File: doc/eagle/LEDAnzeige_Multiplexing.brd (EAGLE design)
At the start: 85.1 x 117.1 mm, 20 parts, among them P1-O8RIGHT TD620831A, P1-P8LEFT TD620831A, U1 SN74HC595N, U2 SN74HC595N, U3 SN74HC595N

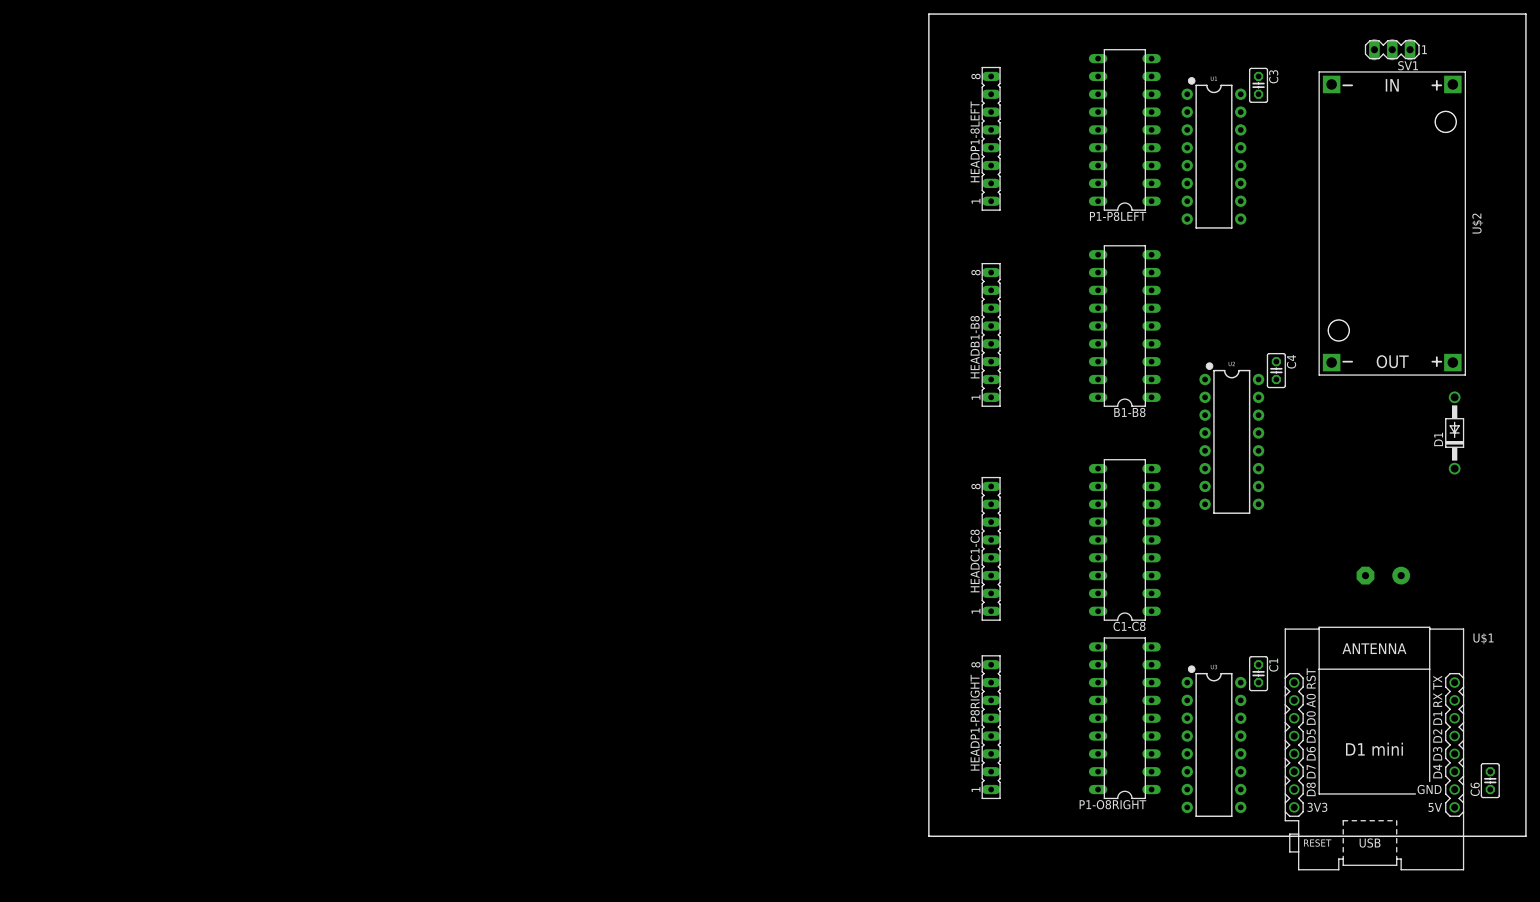
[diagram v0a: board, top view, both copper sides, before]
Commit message: Schematic updated + Refactoring
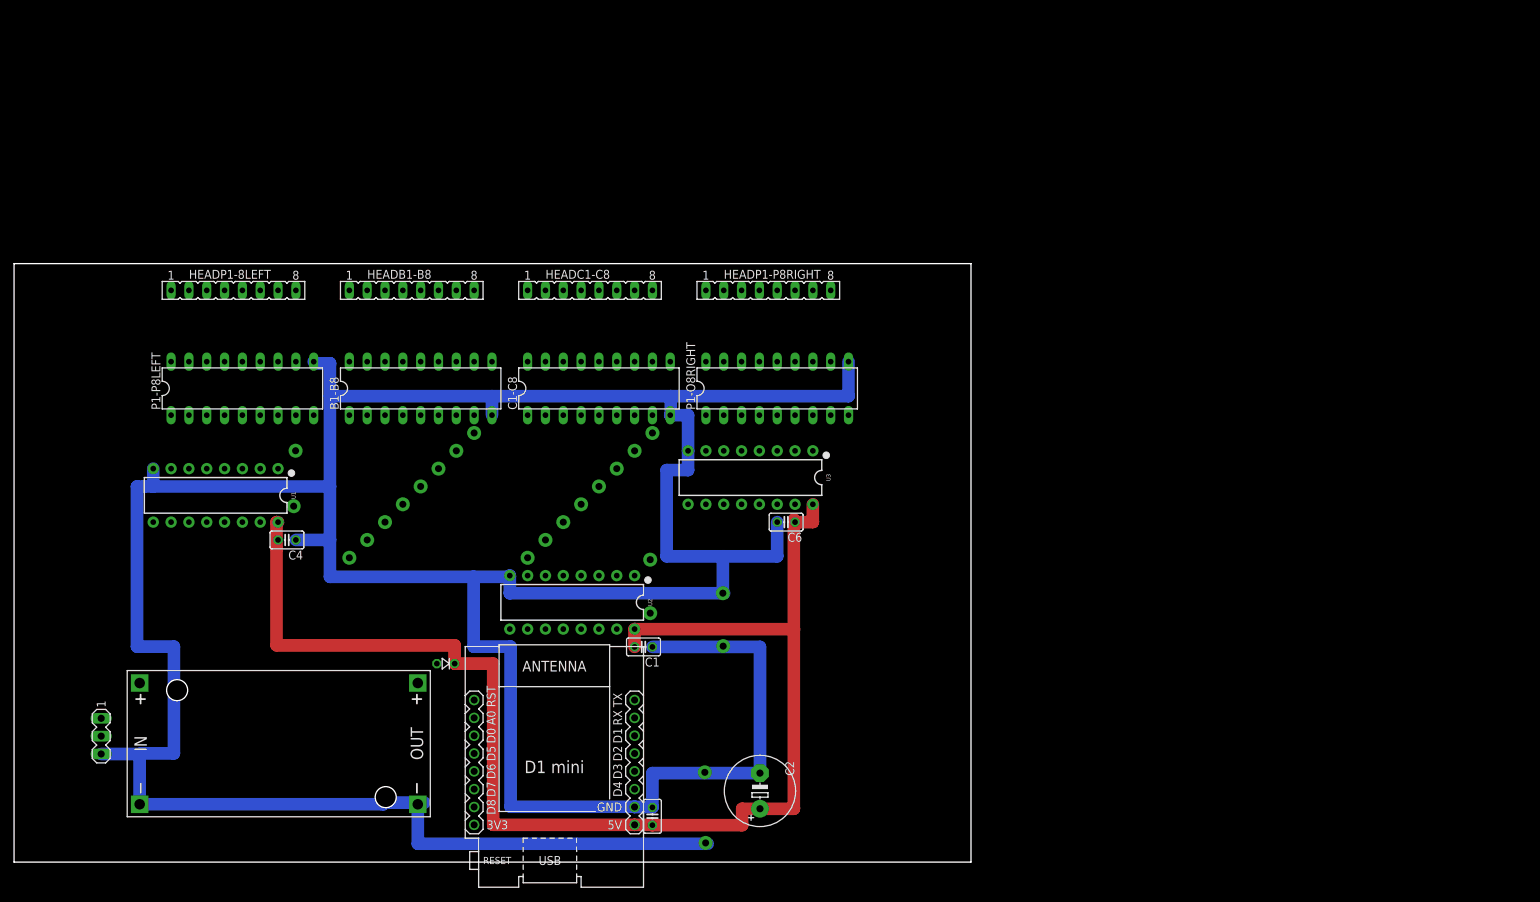
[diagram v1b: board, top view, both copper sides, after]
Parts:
- removed D1: 1N4004, diode:DO41-10
- added 1N4007: (no value), diode:D-2.5
- P1-O8RIGHT, P1-P8LEFT: value TD620831A -> TD627832A
- moved SV1 208.3 mm to (-67.1, 16.5), turned to 270 degrees
- moved U$2 175.1 mm to (-41.8, 15.4), turned to 0 degrees
- moved U1 150.2 mm to (-50.8, 50.8), turned to 180 degrees
- moved C4 143.0 mm to (-40.6, 44.5), turned to 180 degrees
- moved C3 135.3 mm to (11.4, 5.08)
- moved P1-P8LEFT 131.0 mm to (-47.0, 66.0), turned to 0 degrees
- moved U$1 116.9 mm to (-2.54, 12.1)
- moved HEADP1-8LEFT 110.1 mm to (-48.3, 80.0), turned to 0 degrees
- moved C6 106.9 mm to (30.5, 47.0), turned to 180 degrees
- moved B1-B8 100.7 mm to (-21.6, 66.0), turned to 0 degrees
- moved U2 96.7 mm to (0.00, 35.6), turned to 180 degrees
- moved C2 94.0 mm to (26.8, 8.69), flipped to the top, turned to 90 degrees
- moved C1 87.7 mm to (10.2, 29.2), turned to 180 degrees
- moved HEADB1-B8 82.8 mm to (-22.9, 80.0), turned to 0 degrees
- moved C1-C8 78.0 mm to (3.81, 66.0), turned to 0 degrees
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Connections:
- removed net N$38: U$1.JP2.3, U2.12
- removed net N$79: U$1.JP1.3, U1.11, U3.11
- new net N$60: U$1.JP2.4, U2.12
- new net N$76: U$1.JP1.5, U1.11, U3.11
- net 24V: now also P1-O8RIGHT.9, P1-P8LEFT.9; no longer P1-O8RIGHT.10, P1-P8LEFT.10
- net GND: now also P1-O8RIGHT.10, P1-P8LEFT.10; no longer P1-O8RIGHT.9, P1-P8LEFT.9
- net N$34: now also U$1.JP1.3; no longer U$1.JP1.5
- net N$37: now also U$1.JP2.3; no longer U$1.JP2.5
- net N$69: now also 1N4007.A; no longer D1.A
- net N$80: now also U$1.JP2.5; no longer U$1.JP2.4
- net VCC: now also 1N4007.C; no longer D1.C
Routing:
- net GND: track 0.00 -> 463.9 mm
- net VCC: track 0.00 -> 191.0 mm
- net N$63: track 0.00 -> 122.6 mm, vias 0 -> 6
- net 24V: track 0.00 -> 85.1 mm
- net N$76: track 0.00 -> 76.2 mm
- net N$74: track 0.00 -> 71.1 mm
- net N$34: track 0.00 -> 63.5 mm
- net N$61: track 0.00 -> 53.3 mm
- net N$64: track 0.00 -> 50.8 mm, vias 0 -> 3
- net N$3: track 0.00 -> 38.1 mm
- net N$4: track 0.00 -> 35.6 mm
- net N$6: track 20.3 -> 55.9 mm, vias 0 -> 1
- net N$1: track 20.3 -> 53.3 mm, vias 0 -> 1
- net N$80: track 0.00 -> 33.0 mm
- net N$60: track 0.00 -> 27.9 mm
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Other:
- board size 85.1 x 117.1 mm -> 136.3 x 85.3 mm

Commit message: Board updated
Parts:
- moved SV1 61.2 mm to (-69.8, 77.7), turned to 0 degrees
- moved C6 5.08 mm to (30.5, 41.9)
- moved C1 2.54 mm to (10.2, 26.7)
- moved U2 2.54 mm to (0.00, 33.0)
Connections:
- net GND: now also U1.13, U2.13, U3.13
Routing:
- net N$61: track 53.3 -> 91.1 mm
- net N$5: track 10.2 -> 35.6 mm
- net GND: track 463.9 -> 479.1 mm
- net 24V: track 85.1 -> 94.8 mm
- net N$63: track 122.6 -> 127.7 mm
- net N$80: track 33.0 -> 30.4 mm
- net N$7: track 43.2 -> 45.7 mm
- net N$60: track 27.9 -> 25.4 mm
- net N$6: track 55.9 -> 58.4 mm
- net N$4: track 35.6 -> 38.1 mm
- net N$37: track 20.3 -> 17.7 mm
- net N$36: track 13.0 -> 15.6 mm
- net N$3: track 38.1 -> 40.6 mm
- net N$2: track 40.6 -> 43.2 mm
- net N$1: track 53.3 -> 55.9 mm
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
